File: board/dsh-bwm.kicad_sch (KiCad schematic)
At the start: 15 parts, among them IC2 MAX485CSA+T, K1 833H-1C-C-24VDC, K2 833H-1C-C-24VDC, K3 833H-1C-C-24VDC, K4 833H-1C-C-24VDC, Q1 IRLB8721PBF, U1 Pico

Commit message: RP2040 Stamp
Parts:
- removed U1: Pico, MCU_RaspberryPi_and_Boards:RPi_Pico_SMD_TH, symbol MCU_RaspberryPi_and_Boards:Pico
- added J5: SWD6p, symbol Connector_Generic:Conn_02x03_Odd_Even
- added SW1: BOOTSEL, Button_Switch_SMD:SW_SPST_B3U-1000P, symbol Switch:SW_SPST
- added U1: RP2040_Stamp, SamacSys_Parts:RP2040_Stamp_SMD, symbol RP2040_Stamp:RP2040_Stamp
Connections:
- net 3v3: now also U1.34 (3.3V)
- net 5V: now also J5.1 (Pin_1), U1.33 (5V)
- net ALARM: now also U1.8 (GPIO7)
- net COND: now also U1.27 (GPIO26)
- net DE: now also U1.4 (GPIO3)
- net DI: now also U1.5 (GPIO4)
- net GND: now also J5.5 (Pin_5), SW1.1 (A), U1.31 (GND)
- net PSin: now also U1.28 (GPIO27)
- net PSout: now also U1.29 (GPIO28)
- net RE: now also U1.3 (GPIO2)
- net RO: now also U1.6 (GPIO5)
- net ZD: now also U1.7 (GPIO6)
- new net: SW1.2 (B), U1.40 (BOOTSEL)
- new net RESET: J5.3 (Pin_3), U1.39 (~{RESET})
- new net SWCLK: J5.4 (Pin_4), U1.38 (SWCLK)
- new net SWDIO: J5.2 (Pin_2), U1.37 (SWDIO)
- no-connect marks 0 -> 1

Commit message: Power shit and copper fillz boi
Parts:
- removed J5: SWD6p, symbol Connector_Generic:Conn_02x03_Odd_Even
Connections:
- net UART TX: now reaches U1.1 (GPIO0)
- net LDNC: now reaches U1.10 (GPIO9)
- net UART RX: now reaches U1.2 (GPIO1)
- net LDNO: now reaches U1.9 (GPIO8)
- no-connect marks 1 -> 0
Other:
- moved on the sheet: K1, K2, K3, K4, Q1

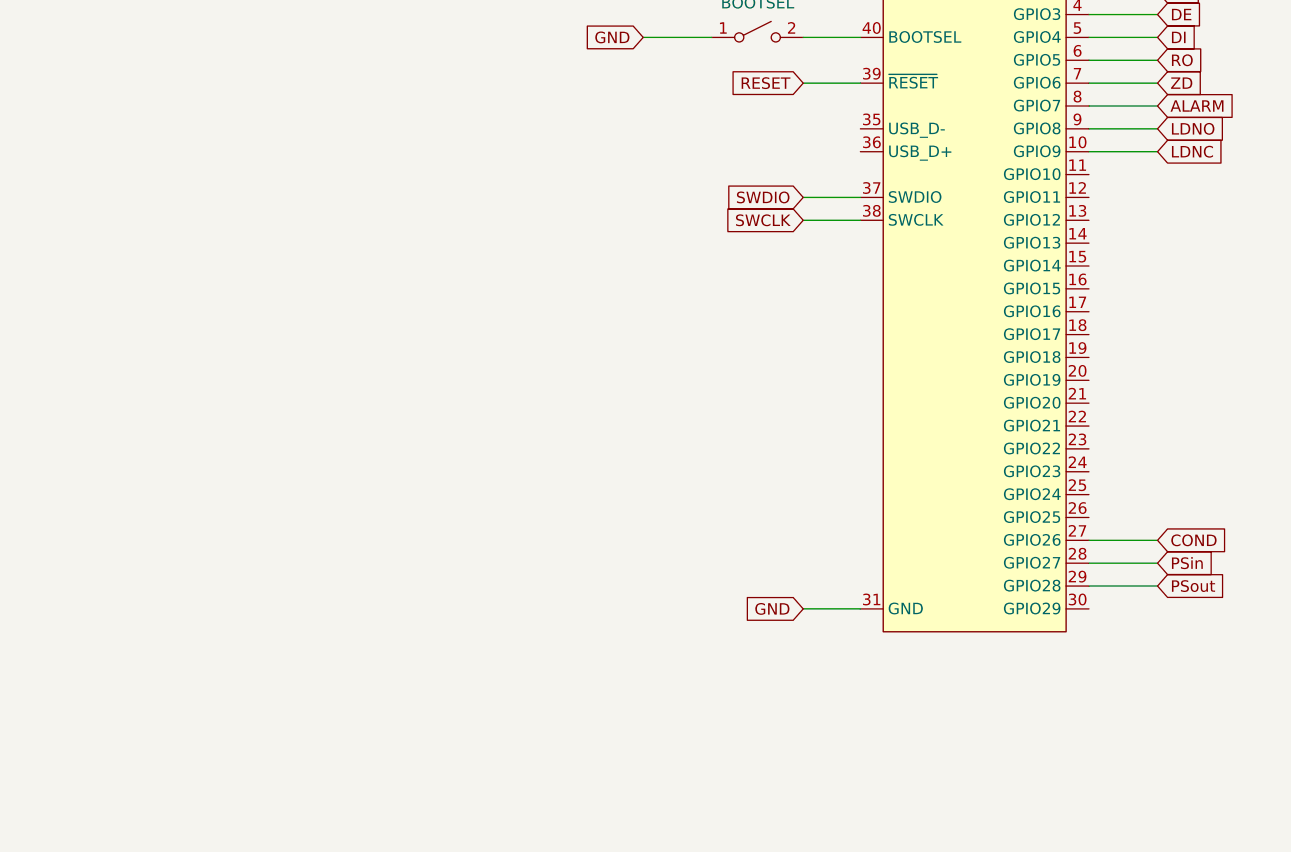
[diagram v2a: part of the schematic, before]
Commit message: board update, modbus address selector
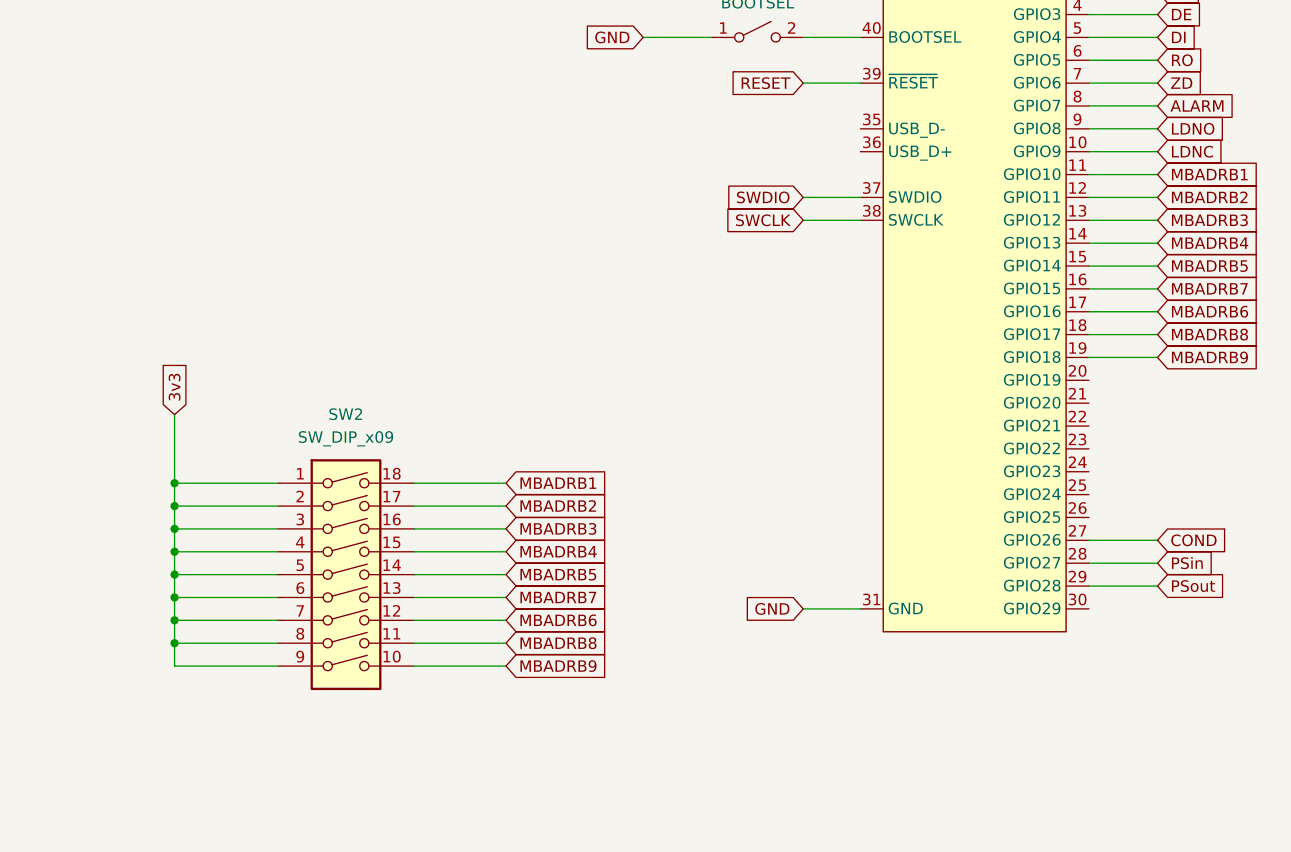
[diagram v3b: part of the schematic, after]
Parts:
- added SW2: SW_DIP_x09, Button_Switch_THT:SW_DIP_SPSTx09_Slide_6.7x24.42mm_W7.62mm_P2.54mm_LowProfile, symbol Switch:SW_DIP_x09
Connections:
- net 3v3: now also SW2.1, SW2.2, SW2.3, SW2.4, SW2.5, SW2.6, SW2.7, SW2.8, SW2.9
- net MBADRB1: now reaches U1.11 (GPIO10)
- net MBADRB1: now also SW2.18
- net MBADRB2: now reaches U1.12 (GPIO11)
- net MBADRB2: now also SW2.17
- net MBADRB3: now reaches U1.13 (GPIO12)
- net MBADRB3: now also SW2.16
- net MBADRB4: now reaches U1.14 (GPIO13)
- net MBADRB4: now also SW2.15
- net MBADRB5: now reaches U1.15 (GPIO14)
- net MBADRB5: now also SW2.14
- net MBADRB7: now reaches U1.16 (GPIO15)
- net MBADRB7: now also SW2.13
- net MBADRB6: now reaches U1.17 (GPIO16)
- net MBADRB6: now also SW2.12
- net MBADRB8: now reaches U1.18 (GPIO17)
- net MBADRB8: now also SW2.11
- net MBADRB9: now reaches U1.19 (GPIO18)
- net MBADRB9: now also SW2.10

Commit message: TPs, vias, some comments on board, fml
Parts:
- removed R1: 1k, Resistor_SMD:R_0805_2012Metric, symbol Device:R_Small
- removed R2: 2k, Resistor_SMD:R_0805_2012Metric, symbol Device:R_Small
- removed SW1: BOOTSEL, Button_Switch_SMD:SW_SPST_B3U-1000P, symbol Switch:SW_SPST
- added IC2: AT24C256C-SSHL-T, SamacSys_Parts:SOIC127P600X175-8N, symbol SamacSys_Parts:AT24C256C-SSHL-T
- added J1: USB_A, Connector_USB:USB_A_Molex_105057_Vertical, symbol Connector:USB_A
- added K1, K6, K7, K8: T81N5D312, SamacSys_Parts:T81H5D31212, symbol SamacSys_Parts:T81N5D312-05
- added Q1, Q2, Q4, Q5, Q6: IRLB8721PBF, SamacSys_Parts:TO254P483X1016X1994-3P, symbol SamacSys_Parts:IRLB8721PBF
- added R5: 10k, Resistor_SMD:R_0805_2012Metric, symbol Device:R_Small
- added R7, R9: 2k, Resistor_SMD:R_0805_2012Metric, symbol Device:R_Small
- added R8: 1k, Resistor_SMD:R_0805_2012Metric, symbol Device:R_Small
- added SW2: RESET, Button_Switch_SMD:SW_SPST_B3U-1000P, symbol Switch:SW_SPST
- added TP1: RO, TestPoint:TestPoint_Pad_D1.5mm, symbol Connector:TestPoint_Small
- added TP10: COND, TestPoint:TestPoint_Pad_D1.5mm, symbol Connector:TestPoint_Small
- added TP11: EEPROMSCL, TestPoint:TestPoint_Pad_D1.5mm, symbol Connector:TestPoint_Small
- added TP12: EEPROMSDA, TestPoint:TestPoint_Pad_D1.5mm, symbol Connector:TestPoint_Small
- added TP13: PSin, TestPoint:TestPoint_Pad_D1.5mm, symbol Connector:TestPoint_Small
- added TP14: D-, TestPoint:TestPoint_Pad_D1.5mm, symbol Connector:TestPoint_Small
- added TP15: D+, TestPoint:TestPoint_Pad_D1.5mm, symbol Connector:TestPoint_Small
- added TP16: PSout, TestPoint:TestPoint_Pad_D1.5mm, symbol Connector:TestPoint_Small
- added TP2: RE, TestPoint:TestPoint_Pad_D1.5mm, symbol Connector:TestPoint_Small
- added TP3: DE, TestPoint:TestPoint_Pad_D1.5mm, symbol Connector:TestPoint_Small
- added TP4: DI, TestPoint:TestPoint_Pad_D1.5mm, symbol Connector:TestPoint_Small
- added TP5: 4-20mA, TestPoint:TestPoint_Pad_D1.5mm, symbol Connector:TestPoint_Small
- added TP6: GND, TestPoint:TestPoint_Pad_D1.5mm, symbol Connector:TestPoint_Small
- added TP7: 24V, TestPoint:TestPoint_Pad_D1.5mm, symbol Connector:TestPoint_Small
- added TP8: B, TestPoint:TestPoint_Pad_D1.5mm, symbol Connector:TestPoint_Small
- added TP9: A, TestPoint:TestPoint_Pad_D1.5mm, symbol Connector:TestPoint_Small
- K2: renamed from K3; value 833H-1C-C-24VDC -> T81N5D312; footprint SamacSys_Parts:833H1CC24VDC -> SamacSys_Parts:T81H5D31212; symbol SamacSys_Parts:833H-1C-C-24VDC -> SamacSys_Parts:T81N5D312-05; Arrow Part Number (none) -> T81N5D312-05; Arrow Price/Stock (none) -> https://www.arrow.com/en/products/t81n5d312-05/te-connectiv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; Height 15.5 -> 11.7; Manufacturer_Name Song Chuan -> TE Connectivity; Manufacturer_Part_Number 833H-1C-C-24VDC -> T81N5D312-05; Mouser Part Number 893-833H-1C-C-24VDC -> 655-T81N5D312-05; Mouser Price/Stock https://www.mouser.co.uk/ProductDetail/Song-Chuan/833H-1C-C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 -> https://www.mouser.co.uk/ProductDetail/TE-Connectivity-PB/T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
- K3: renamed from K1; value 833H-1C-C-24VDC -> T81N5D312; footprint SamacSys_Parts:833H1CC24VDC -> SamacSys_Parts:T81H5D31212; symbol SamacSys_Parts:833H-1C-C-24VDC -> SamacSys_Parts:T81N5D312-05; Arrow Part Number (none) -> T81N5D312-05; Arrow Price/Stock (none) -> https://www.arrow.com/en/products/t81n5d312-05/te-connectiv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; Height 15.5 -> 11.7; Manufacturer_Name Song Chuan -> TE Connectivity; Manufacturer_Part_Number 833H-1C-C-24VDC -> T81N5D312-05; Mouser Part Number 893-833H-1C-C-24VDC -> 655-T81N5D312-05; Mouser Price/Stock https://www.mouser.co.uk/ProductDetail/Song-Chuan/833H-1C-C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 -> https://www.mouser.co.uk/ProductDetail/TE-Connectivity-PB/T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
- K4: renamed from K2; value 833H-1C-C-24VDC -> T81N5D312; footprint SamacSys_Parts:833H1CC24VDC -> SamacSys_Parts:T81H5D31212; symbol SamacSys_Parts:833H-1C-C-24VDC -> SamacSys_Parts:T81N5D312-05; Arrow Part Number (none) -> T81N5D312-05; Arrow Price/Stock (none) -> https://www.arrow.com/en/products/t81n5d312-05/te-connectiv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; Height 15.5 -> 11.7; Manufacturer_Name Song Chuan -> TE Connectivity; Manufacturer_Part_Number 833H-1C-C-24VDC -> T81N5D312-05; Mouser Part Number 893-833H-1C-C-24VDC -> 655-T81N5D312-05; Mouser Price/Stock https://www.mouser.co.uk/ProductDetail/Song-Chuan/833H-1C-C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 -> https://www.mouser.co.uk/ProductDetail/TE-Connectivity-PB/T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
- K5: renamed from K4; value 833H-1C-C-24VDC -> T81N5D312; footprint SamacSys_Parts:833H1CC24VDC -> SamacSys_Parts:T81H5D31212; symbol SamacSys_Parts:833H-1C-C-24VDC -> SamacSys_Parts:T81N5D312-05; Arrow Part Number (none) -> T81N5D312-05; Arrow Price/Stock (none) -> https://www.arrow.com/en/products/t81n5d312-05/te-connectiv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; Height 15.5 -> 11.7; Manufacturer_Name Song Chuan -> TE Connectivity; Manufacturer_Part_Number 833H-1C-C-24VDC -> T81N5D312-05; Mouser Part Number 893-833H-1C-C-24VDC -> 655-T81N5D312-05; Mouser Price/Stock https://www.mouser.co.uk/ProductDetail/Song-Chuan/833H-1C-C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 -> https://www.mouser.co.uk/ProductDetail/TE-Connectivity-PB/T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
- R4: value 1k -> 10k; JLC (none) -> 0402WGF1500TCE
- R6: value 2k -> 1k
- SW1: renamed from SW2; value SW_DIP_x09 -> ModBus address selector; footprint Button_Switch_THT:SW_DIP_SPSTx09_Slide_6.7x24.42mm_W7.62mm_P2.54mm_LowProfile -> Button_Switch_THT:SW_DIP_SPSTx07_Slide_6.7x19.34mm_W7.62mm_P2.54mm_LowProfile; symbol Switch:SW_DIP_x09 -> Switch:SW_DIP_x07
- renumbered IC2 to IC1, Q1 to Q3, R3 to R1, R5 to R2, R9 to R3
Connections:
- net 24V: now also K5.3 (COM), Q1.3, Q2.3, Q4.3, Q5.3, Q6.3, TP7.1; no longer K5.1 (COM)
- net 3v3: now also K2.3 (COM); no longer K2.1 (COM), SW1.8, SW1.9
- net 4-20mA input: now also TP5.1
- net 5V: now also R4.1, IC2.8 (VCC), R5.1
- net A: now also TP9.1
- net ALARM: now also U1.20 (GPIO19); no longer U1.8 (GPIO7)
- net B: now also TP8.1
- net COND: now also TP10.1
- net DE: now also TP3.1
- net DI: now also TP4.1
- net G: now also K5.2 (NO); no longer K5.3 (NO)
- net GND: now also IC2.4 (GND), J1.4 (GND), J1.5 (Shield), K1.5 (COIL_2), K6.5 (COIL_2), K7.5 (COIL_2), K8.5 (COIL_2), R7.1, R9.1, SW2.1 (A), TP6.1; no longer R6.1
- net LDNC: now also U1.9 (GPIO8); no longer U1.10 (GPIO9)
- net LDNO: now also U1.8 (GPIO7); no longer U1.9 (GPIO8)
- net MBADRB1: now also SW1.8, U1.13 (GPIO12); no longer SW1.18, U1.11 (GPIO10)
- net MBADRB2: now also SW1.9, U1.14 (GPIO13); no longer SW1.17, U1.12 (GPIO11)
- net MBADRB3: now also SW1.10, U1.15 (GPIO14); no longer SW1.16, U1.13 (GPIO12)
- net MBADRB4: now also SW1.11, U1.16 (GPIO15); no longer SW1.15, U1.14 (GPIO13)
- net MBADRB5: now also SW1.12, U1.17 (GPIO16); no longer SW1.14, U1.15 (GPIO14)
- net MBADRB6: now also SW1.13, U1.18 (GPIO17); no longer SW1.12, U1.17 (GPIO16)
- net MBADRB7: now also SW1.14, U1.19 (GPIO18); no longer SW1.13, U1.16 (GPIO15)
- net PSin: now also R6.2, R7.2, TP13.1
- net PSout: now also R8.2, R9.2, TP16.1; no longer R4.2, R6.2
- net PressureIN: now also R6.1
- net PressureOUT: now also R8.1; no longer R4.1
- net R: now also K5.1 (NC); no longer K5.4 (NC)
- net RE: now also TP2.1
- net RO: now also TP1.1
- net ZD: now also K2.2 (NO); no longer K2.3 (NO)
- net ZDSENSE: now also K2.4 (COIL_1); no longer K2.2 (COIL_1)
- net ALARMLEK: now reaches U1.21 (GPIO20)
- net ALARMLEK: now also Q2.1
- net ALARMZOUT: now reaches U1.22 (GPIO21)
- net ALARMZOUT: now also Q6.1
- net ALARMDRUKIN: now reaches U1.23 (GPIO22)
- net ALARMDRUKIN: now also Q5.1
- net ALARMDRUKUIT: now reaches U1.24 (GPIO23)
- net ALARMDRUKUIT: now also Q1.1
- net ALARMCOND: now reaches U1.25 (GPIO24)
- net ALARMCOND: now also Q4.1
- net at U1.35 (USB_D-): now also J1.2 (D-), TP14.1
- net at U1.36 (USB_D+): now also J1.3 (D+), TP15.1
- net AlarmC1 renamed LekNC
- net AlarmC2 renamed AlarmNC
- net AlarmNC1: no longer names the net of K3.4 (COIL_1)
- net AlarmNC1: now also Q2.2
- net AlarmNC2: no longer names the net of K4.4 (COIL_1)
- net AlarmNC2: now also K5.4 (COIL_1), Q3.2
- net AlarmNO1 renamed LekC
- net AlarmNO2 renamed AlarmC
- removed net MBADRB8: SW1.11, U1.18 (GPIO17)
- removed net MBADRB9: SW1.10, U1.19 (GPIO18)
- net RESET: no longer names the net of U1.39 (~{RESET})
- net RESET: now also SW2.2 (B)
- new net: K6.4 (COIL_1), Q4.2
- new net: K8.4 (COIL_1), Q6.2
- new net: K1.4 (COIL_1), Q1.2
- new net: K7.4 (COIL_1), Q5.2
- new net AlarmNO: K4.2 (NO)
- new net CondC: K6.3 (COM)
- new net CondNC: K6.1 (NC)
- new net CondNO: K6.2 (NO)
- new net DrukInC: K7.3 (COM)
- new net DrukInNC: K7.1 (NC)
- new net DrukInNO: K7.2 (NO)
- new net DrukUitC: K1.3 (COM)
- new net DrukUitNC: K1.1 (NC)
- new net DrukUitNO: K1.2 (NO)
- new net EEPROMSCL: IC2.6 (SCL), R5.2, TP11.1, U1.12 (GPIO11)
- new net EEPROMSDA: IC2.5 (SDA), R4.2, TP12.1, U1.11 (GPIO10)
- new net LekNO: K3.2 (NO)
- new net ZoutC: K8.3 (COM)
- new net ZoutNC: K8.1 (NC)
- new net ZoutNO: K8.2 (NO)
- no-connect marks 0 -> 1
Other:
- moved on the sheet: D1, K2, K3, K4, K5, Q3, R1, R2, U1

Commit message: pushpushpush
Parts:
- removed SW2: RESET, Button_Switch_SMD:SW_SPST_B3U-1000P, symbol Switch:SW_SPST
- added D3: LED_Small, LED_SMD:LED_0603_1608Metric, symbol Device:LED_Small
- added R3: 470, Resistor_SMD:R_0805_2012Metric, symbol Device:R_Small
- TP10: renamed from TP11; value EEPROMSCL -> ESCL
- TP17: renamed from TP12; value EEPROMSDA -> ESDA
- renumbered D1 to D2, IC1 to IC3, J1 to J3, K5 to K1, K4 to K3, K3 to K4, K8 to K5, K7 to K6, K1 to K7, K6 to K8, Q5 to Q1, Q6 to Q2, Q1 to Q3, Q2 to Q4, Q4 to Q5, Q3 to Q6, R3 to R10, R4 to R11, R5 to R12, R8 to R4, R1 to R5, R9 to R6, R2 to R8, R6 to R9, TP7 to TP1, TP2 to TP11, TP1 to TP12, TP5 to TP13, TP10 to TP14, TP8 to TP15, TP9 to TP16, TP6 to TP3, TP14 to TP4, TP16 to TP5, TP15 to TP6, TP13 to TP7, TP3 to TP8, TP4 to TP9
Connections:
- net ALARMCOND: now also U1.26 (GPIO25); no longer U1.25 (GPIO24)
- net ALARMDRUKIN: now also U1.24 (GPIO23); no longer U1.23 (GPIO22)
- net ALARMDRUKUIT: now also U1.25 (GPIO24); no longer U1.24 (GPIO23)
- net ALARMZOUT: now also U1.23 (GPIO22); no longer U1.22 (GPIO21)
- net GND: now also D3.1 (K)
- net at U1.10 (GPIO9): now also R3.2
- new net: D3.2 (A), R3.1
- no-connect marks 1 -> 3
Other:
- moved on the sheet: J3, TP4, TP6
